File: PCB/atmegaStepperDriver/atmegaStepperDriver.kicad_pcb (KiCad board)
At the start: 2 copper layers, 50.8 x 92.1 mm, 81 parts, among them J1 General power, J2 Motor Output, J3 Motor power, J4 Conn_01x02_Pin, J5 Reset Header, J6 I2C Communication pins, J8 Conn_01x06_Socket, J9 Stepper communication pins, Q1 TIP42C, Q10 BC547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

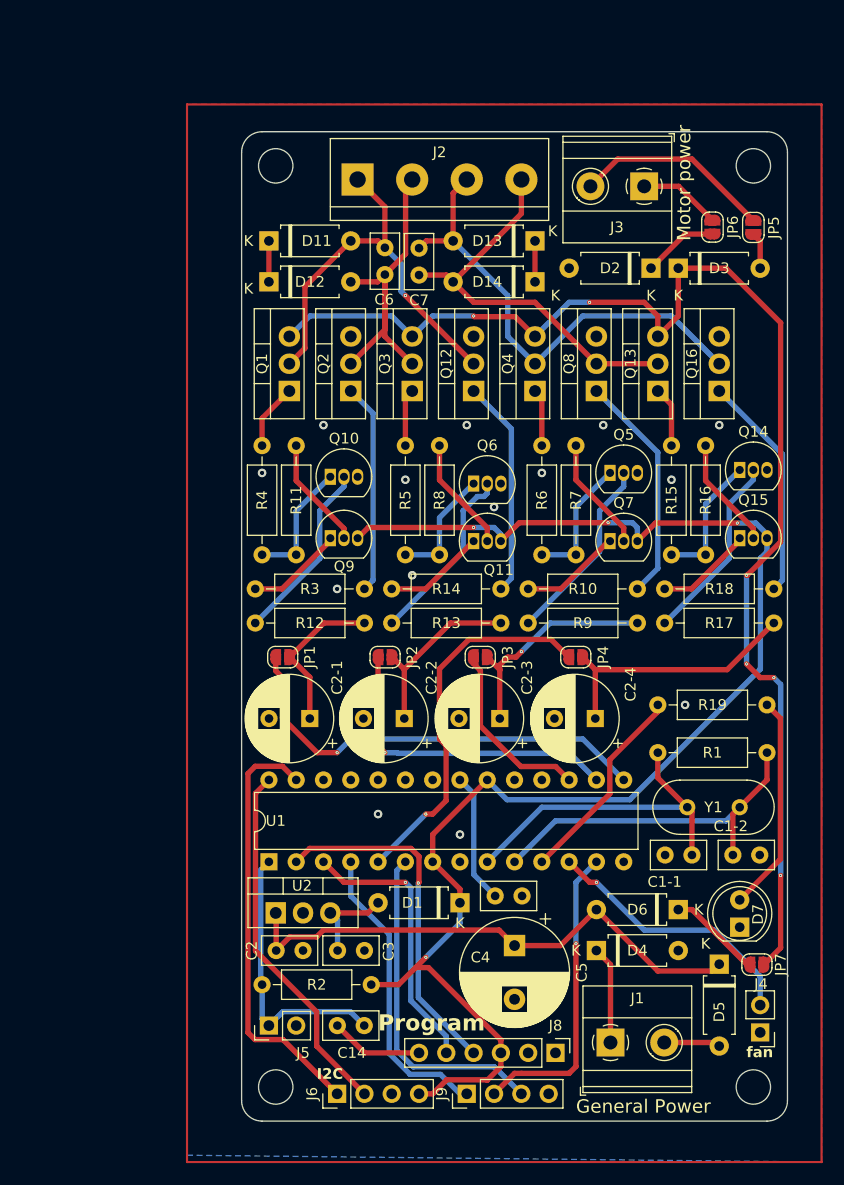
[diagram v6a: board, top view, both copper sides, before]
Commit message: added transistor for fan; final checks; Gerber files ready; V0.8.2
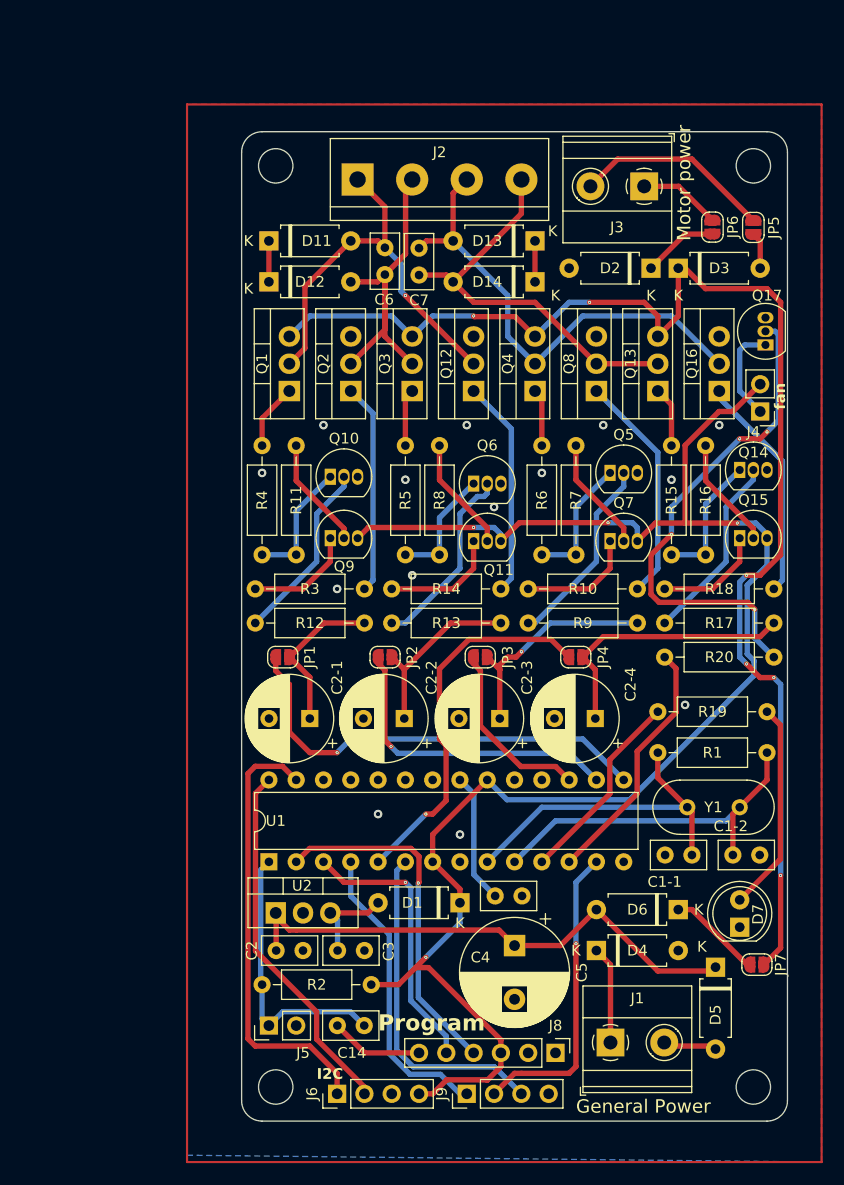
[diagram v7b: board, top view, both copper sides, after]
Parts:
- added Q17: BC547, Package_TO_SOT_THT:TO-92_Inline, F.Cu at (121.1, 71.9)
- added R20: 50, Resistor_THT:R_Axial_DIN0207_L6.3mm_D2.5mm_P10.16mm_Horizontal, F.Cu at (111.8, 101.0)
- moved J4 57.8 mm to (120.7, 78.1)
- moved R19 0.64 mm to (111.1, 106.0)
- moved D5 0.44 mm to (116.5, 129.8)
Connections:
- J4 pad 1: GND -> Net-(J4-Pin_1)
- J4 pad 2: Fan -> +5V
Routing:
- net Net-(Q17-B): track 0.00 -> 46.9 mm, vias 0 -> 4
- net +5V: track 135.7 -> 152.8 mm
- net Net-(J4-Pin_1): track 0.00 -> 9.10 mm
- net Motor Power: track 123.7 -> 126.1 mm
- net Net-(Q11-C): track 9.46 -> 10.9 mm
- net Net-(Q7-C): track 9.46 -> 10.9 mm
- net SDA: track 40.1 -> 41.5 mm
- net Fan: track 24.9 -> 23.6 mm, vias 1 -> 0
- net Net-(Q15-C): track 9.07 -> 10.2 mm
- net Net-(Q9-C): track 9.07 -> 10.2 mm
- net Net-(Q6-B): track 17.0 -> 17.8 mm
- net Gate 4: track 24.6 -> 25.3 mm
- net Net-(JP2-B): track 29.9 -> 29.2 mm
- net Net-(U1-PD5): track 19.1 -> 18.4 mm
- net Net-(D7-A): track 20.2 -> 19.6 mm

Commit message: changed version on board back
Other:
- board text added: "atMega Stepper Driver V0.8.2"
- board text removed: "atMega Stepper Driver V0.8.0"
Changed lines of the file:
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@@
   (gr_line (start 72.39 142.24) (end 72.39 53.975)
     (stroke (width 0.1) (type default)) (layer "Edge.Cuts"))
-  (gr_text "atMega Stepper Driver V0.8.0" (at 108.533758 117.135771) (layer "B.SilkS")
+  (gr_text "atMega Stepper Driver V0.8.2" (at 108.533758 117.135771) (layer "B.SilkS")
     (effects (font (size 1.5 1.5) (thickness 0.3) bold) (justify left bottom mirror))
   )
